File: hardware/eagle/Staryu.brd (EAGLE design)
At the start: 57.1 x 38.1 mm, 29 parts, among them IC1 ATMEGA32U2-TQFP, SW1 CHERRY-MX-LED, SW2 CHERRY-MX-LED, SW3 CHERRY-MX-LED, SW4 CHERRY-MX-LED, SW5 CHERRY-MX-LED, Y1 16MHZ

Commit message: Update eagle files and schematics to v1.2 - Change 3 LEDs on top side to WS2812B
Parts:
- removed D2, D3: (no value), SparkFun-LED:LED-1206
- removed R10, R11, R9: 330, SparkFun-Resistors:0603-RES
- added C5: 0.1uF, SparkFun-Capacitors:0603-CAP
- D1: value (none) -> WS2812B; device SparkFun-LED:LED-1206 -> SparkFun-LED:WS2812B
- JP2: value (none) -> AVR_ISP
- moved LOGO1 30.7 mm to (47.6, 19.1), flipped to the bottom
- moved D1 4.49 mm to (9.53, 25.4), turned to 180 degrees
- moved C2 0.64 mm to (17.8, 35.6)
- moved JP1 0.63 mm to (9.53, 36.8)
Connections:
- removed net N$20: IC1.19, R10.1
- removed net N$21: IC1.20, R9.1
- removed net N$27: D3.C, R11.2
- removed net N$28: D2.C, R10.2
- removed net N$29: D1.C, R9.2
- net 5V: now also C5.1, D1.1; no longer D1.A, D2.A, D3.A
- net GND: now also C5.2, D1.3
- net N$19: now also D1.4, IC1.21; no longer IC1.18, R11.1
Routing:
- net GND: track 185.2 -> 191.6 mm, vias 4 -> 5
- net N$20: track 5.64 -> 0.00 mm, vias 1 -> 0
- net N$19: track 9.91 -> 5.17 mm
- net N$21: track 4.18 -> 0.00 mm, vias 1 -> 0
- net 5V: track 192.6 -> 189.1 mm, vias 3 -> 4
- net N$29: track 2.09 -> 0.00 mm
- net N$28: track 2.09 -> 0.00 mm
- net N$27: track 2.09 -> 0.00 mm
- net N$3: track 4.64 -> 5.20 mm
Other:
- board text added: "Staryu v1.1"

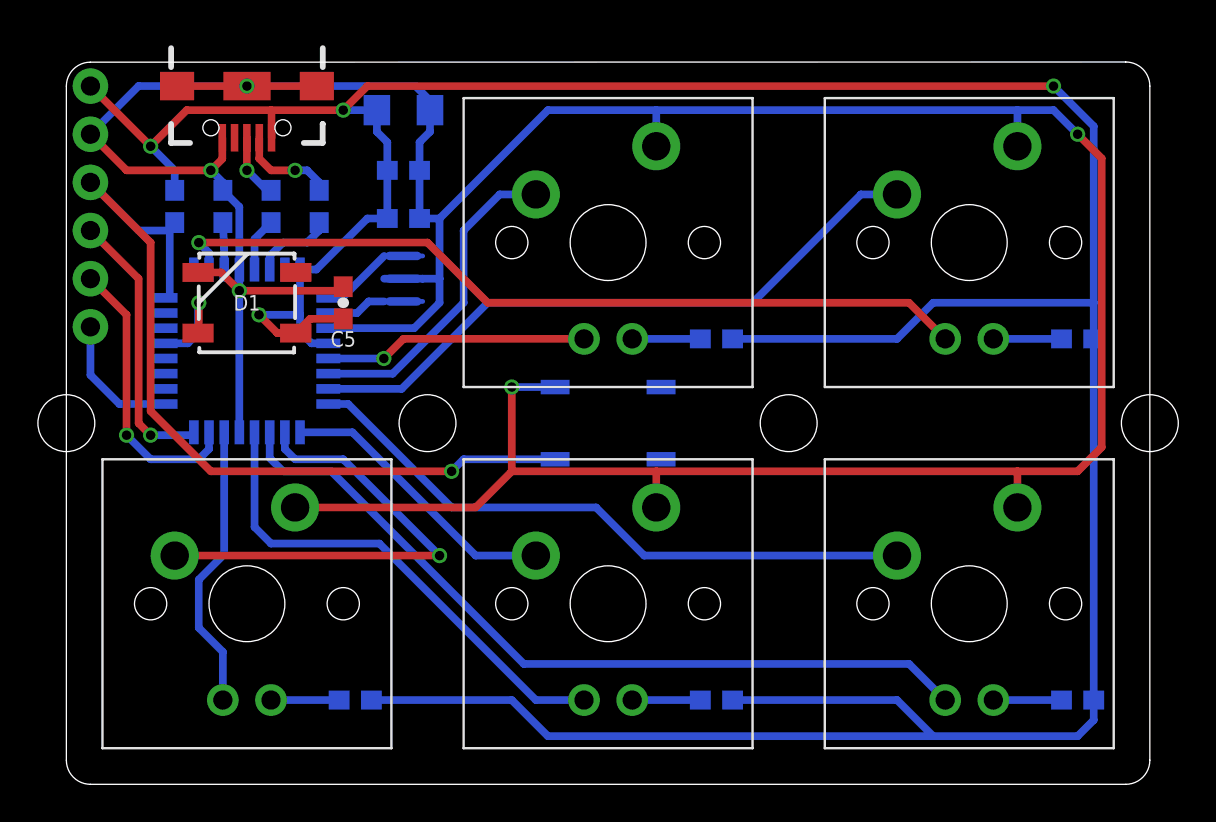
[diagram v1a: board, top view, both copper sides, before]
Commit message: Update eagle files and schematics to v1.2 - Compact outline - Relocate LED and re-route circuits - Add logos
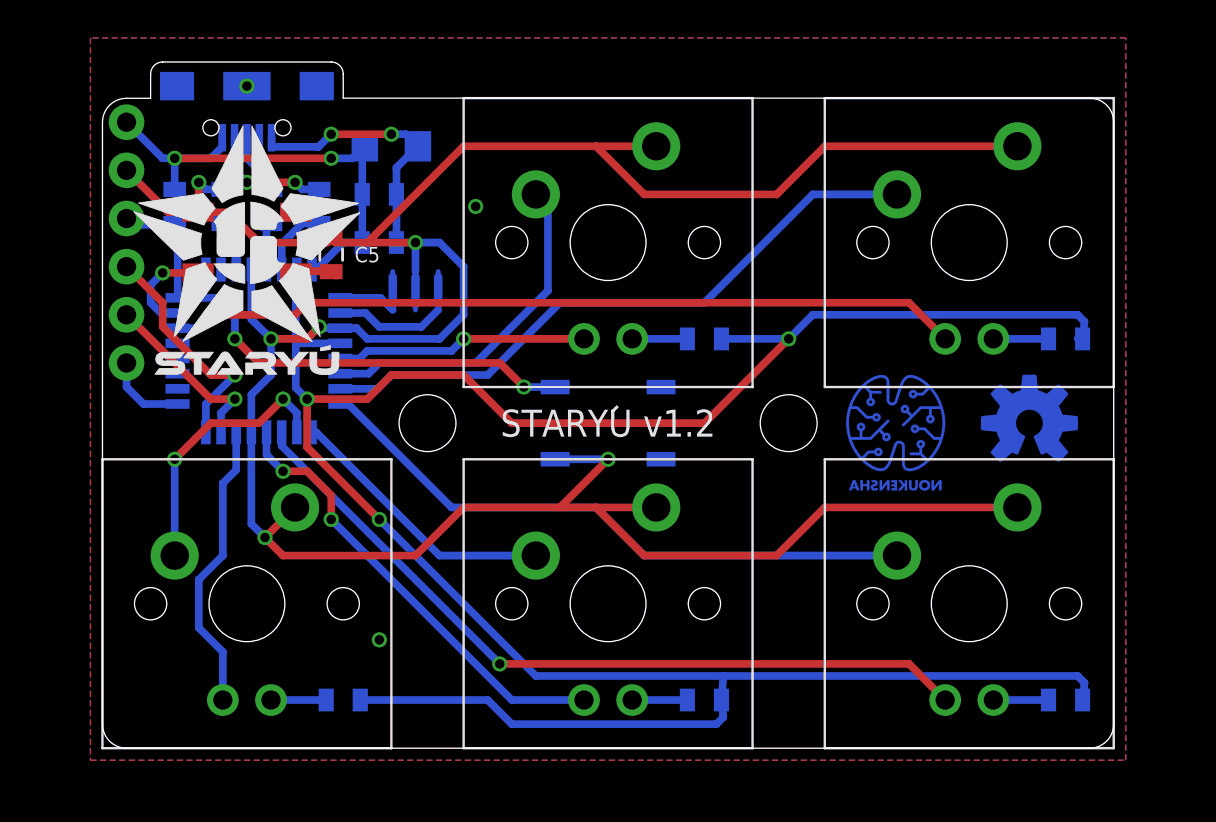
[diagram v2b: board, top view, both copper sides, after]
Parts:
- removed IC1: ATMEGA32U2-TQFP, adafruit:TQFP32-08
- added LOGO2: NOUKENSHA-LOGOM, Noukensha:NOUKENSHA-LOGO-M
- added LOGO3: OSHW-LOGOM, Noukensha:OSHW-LOGO-M
- added U$3: CC-BY-SANIX, cc-by-sa:CC-BY-SA_NIX
- added U1: ATMEGA32U2-TQFP, adafruit:TQFP32-08
- C1, C3, C4, C5: device SparkFun-Capacitors:0603-CAP -> SparkFun-Capacitors:0805
- D1: device SparkFun-LED:WS2812B -> ws2812:WS2812B_NOSILK
- LOGO1: value OSHW-LOGOM -> STARYU-LOGO; device SparkFun-Aesthetics:OSHW-LOGO-M -> Noukensha:STARYU-LOGO
- R1, R2, R3, R4, R5, R6, R7, R8: device SparkFun-Resistors:0603-RES -> SparkFun-Resistors:0805
- moved LOGO1 39.3 mm to (9.53, 28.6), flipped to the top
- moved D1 3.18 mm to (9.53, 28.6)
- moved JP2 2.69 mm to (3.17, 34.9)
- moved C5 2.62 mm to (14.0, 27.9)
- moved C2 2.01 mm to (17.1, 33.7)
- moved C3 1.80 mm to (16.5, 31.1)
- moved C4 1.80 mm to (16.5, 28.6)
- moved Y1 0.90 mm to (18.4, 26.0), turned to 180 degrees
- moved R5 0.64 mm to (52.7, 23.5)
- moved R6 0.64 mm to (52.7, 4.45)
- moved R8 0.63 mm to (14.6, 4.45)
- moved R4 0.63 mm to (33.7, 23.5)
- moved R7 0.63 mm to (33.7, 4.45)
- flipped JP1 to the bottom
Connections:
- new net SHIELD: JP1.SHIELD1, JP1.SHIELD2, JP1.SHIELD3
- net 5V: now also U1.31, U1.32, U1.4; no longer IC1.31, IC1.32, IC1.4
- net GND: now also S1.1, U1.13, U1.28, U1.3; no longer IC1.13, IC1.28, IC1.3, JP1.SHIELD1, JP1.SHIELD2, JP1.SHIELD3, S1.3
- net MISO: now also U1.17; no longer IC1.17
- net MOSI: now also U1.16; no longer IC1.16
- net N$1: now also U1.29; no longer IC1.29
- net N$14: now also U1.6; no longer IC1.6
- net N$15: now also U1.7; no longer IC1.7
- net N$16: now also U1.8; no longer IC1.8
- net N$17: now also U1.9; no longer IC1.9
- net N$18: now also U1.10; no longer IC1.10
- net N$19: now also U1.23; no longer IC1.21
- net N$2: now also U1.30; no longer IC1.30
- net N$30: now also U1.12; no longer IC1.12
- net N$31: now also U1.22; no longer IC1.26
- net N$32: now also U1.11; no longer IC1.11
- net N$33: now also U1.14; no longer IC1.14
- net N$34: now also U1.5; no longer IC1.5
- net N$5: now also U1.1; no longer IC1.1
- net N$6: now also U1.2; no longer IC1.2
- net N$7: now also U1.27; no longer IC1.27
- net N$8: now also S1.3, U1.24; no longer IC1.24, S1.1
- net SCK: now also U1.15; no longer IC1.15
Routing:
- net 5V: track 189.1 -> 161.7 mm, vias 4 -> 6
- net GND: track 191.6 -> 165.8 mm, vias 5 -> 8
- net N$8: track 45.9 -> 29.2 mm, vias 1 -> 2
- net N$18: track 25.3 -> 14.2 mm, vias 1 -> 2
- net SCK: track 15.0 -> 9.61 mm
- net MISO: track 7.25 -> 4.33 mm
- net N$6: track 3.20 -> 5.83 mm
- net N$30: track 26.2 -> 24.0 mm, vias 0 -> 2
- net MOSI: track 14.5 -> 12.5 mm
- net N$3: track 5.20 -> 6.60 mm, vias 1 -> 2
- net N$31: track 43.1 -> 41.8 mm
- net N$32: track 42.3 -> 41.3 mm, vias 0 -> 1
- net N$14: track 17.1 -> 18.1 mm
- net N$5: track 3.86 -> 3.03 mm
- net N$11: track 3.59 -> 2.91 mm
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- added copper zone on layer 1, net SHIELD
- added copper zone on layer 16, net SHIELD
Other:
- board size 57.1 x 38.1 mm -> 53.3 x 36.2 mm
- board text added: "STARYU v1.2"
- board text removed: "Staryu v1.1"

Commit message: Update eagle files and schematics to v1.3 - Contract outline even more - Change logo to exposing copper - Change footprint of resonator to be easier to solder
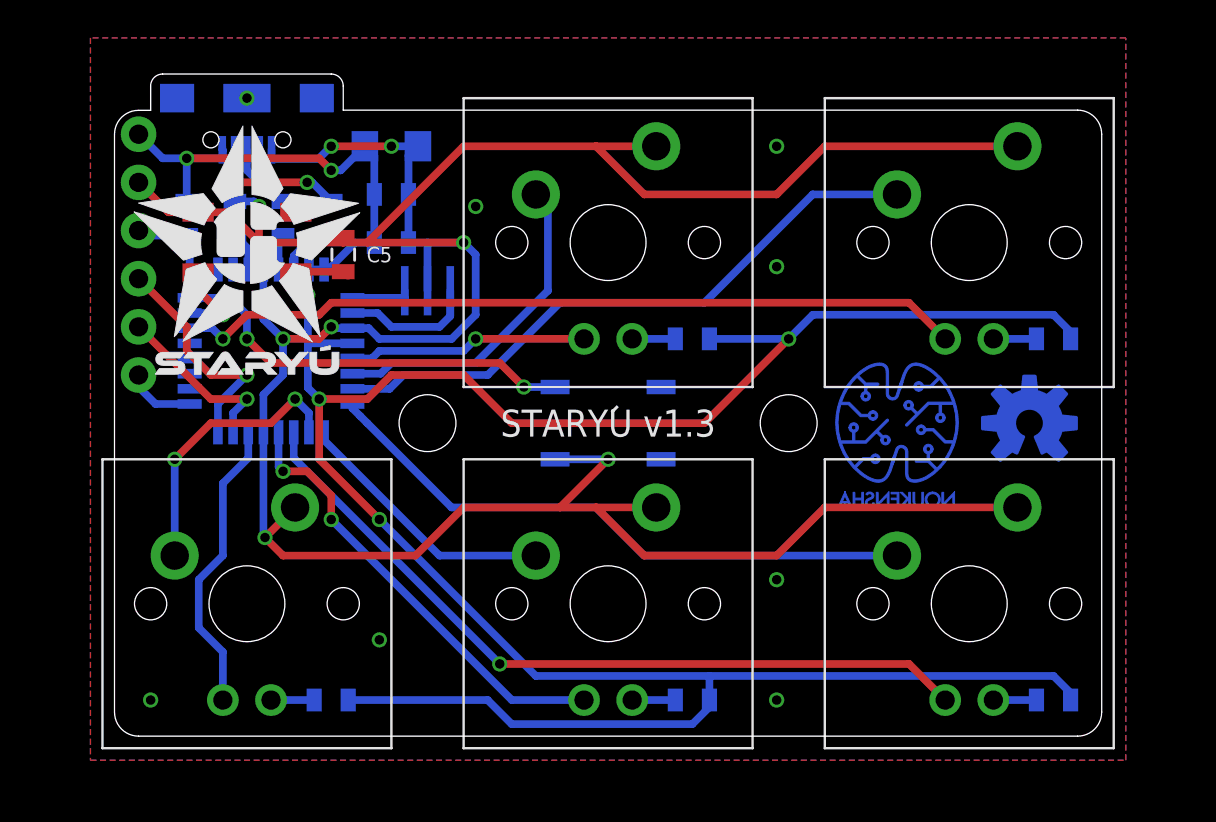
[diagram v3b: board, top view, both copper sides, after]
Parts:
- LOGO1: value STARYU-LOGO -> STARYU_LOGO; device Noukensha:STARYU-LOGO -> Noukensha:STARYU_LOGO
- LOGO2: value NOUKENSHA-LOGOM -> NOUKENSHA_LOGO.3_EXP; device Noukensha:NOUKENSHA-LOGO-M -> Noukensha:NOUKENSHA_LOGO_COPPER_EXPOSED_.3
- LOGO3: value OSHW-LOGOM -> OSHW_LOGOM_EXP; device Noukensha:OSHW-LOGO-M -> Noukensha:OSHW_LOGO_COPPER_EXPOSED_M
- Y1: device SparkFun-FreqCtrl:RESONATOR-SMD -> cstce-resonator:CSTER12M
- moved C1 0.90 mm to (8.89, 29.8)
- moved R1 0.90 mm to (14.0, 29.8)
- moved R2 0.90 mm to (11.4, 29.8)
- moved R3 0.90 mm to (6.35, 29.8)
- moved JP2 0.90 mm to (3.81, 34.3)
- moved Y1 0.64 mm to (19.1, 26.0)
- moved C5 0.63 mm to (14.6, 27.9)
- moved R8 0.63 mm to (14.0, 4.45)
- moved U1 0.63 mm to (10.8, 22.9)
- moved C3 0.63 mm to (17.1, 31.1)
- moved C4 0.63 mm to (17.1, 28.6)
- moved JP1 0.63 mm to (9.53, 36.2)
- moved R4 0.63 mm to (33.0, 23.5)
- moved R5 0.63 mm to (52.1, 23.5)
- moved R6 0.63 mm to (52.1, 4.45)
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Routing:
- net GND: track 165.8 -> 168.3 mm
- net 5V: track 161.7 -> 159.6 mm
- net N$8: track 29.2 -> 28.0 mm
- net N$6: track 5.83 -> 7.04 mm
- net N$19: track 5.35 -> 4.54 mm
- net N$9: track 2.91 -> 2.27 mm
- net N$12: track 2.91 -> 2.27 mm
- net MISO: track 4.33 -> 3.70 mm
- net N$34: track 13.3 -> 12.6 mm
- net N$14: track 18.1 -> 17.5 mm
- net N$13: track 2.91 -> 2.28 mm
- net N$7: track 2.72 -> 2.08 mm
- net N$1: track 2.50 -> 1.87 mm
- net N$2: track 3.77 -> 3.14 mm
- net N$18: track 14.2 -> 14.8 mm
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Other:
- board size 53.3 x 36.2 mm -> 52.1 x 34.9 mm
- board text added: "STARYU v1.3"
- board text removed: "STARYU v1.2"

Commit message: Update hardware to v1.4 - Support both of ATMEGA32U2-AU (32-TQFP) and ATMEGA32U2-MU (32-QFN) - Support both of normal and reverse mounting switch (selected by jumper) - Replace Micro USB connector with a much tougher one - Add a new DOUT connector exported from WS2812B - Correct name and value of Y1 - Change logo
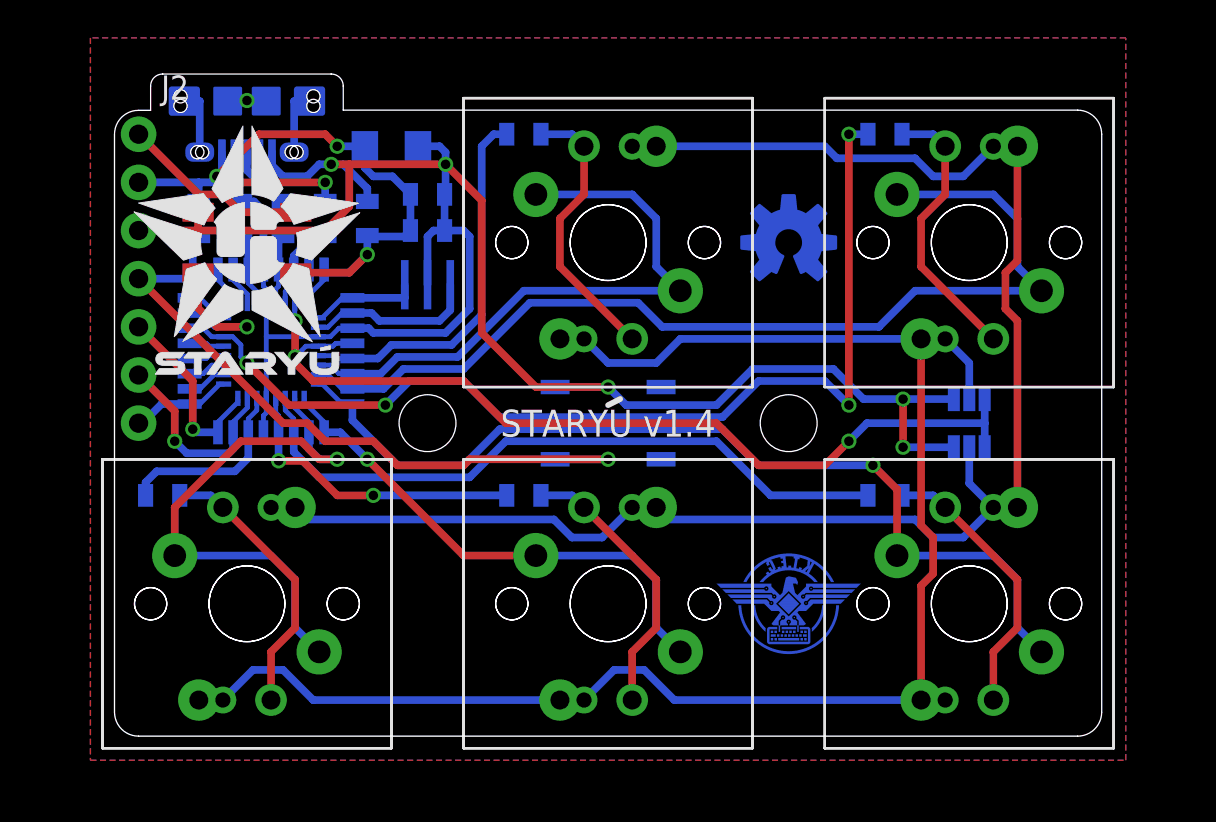
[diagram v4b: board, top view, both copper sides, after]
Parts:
- removed LOGO2: NOUKENSHA_LOGO.3_EXP, Noukensha:NOUKENSHA_LOGO_COPPER_EXPOSED_.3
- added IC1: ATMEGA32U2-QFN, atmega32u2:QFN32
- added J1: MYCON2_USB-MINI-B, usb-micro-b:CON2_USB_MICRO_B_AT
- added J2: (no value), SparkFun-Connectors:1X01_NO_SILK
- added J3: AVR_ISP, SparkFun-Connectors:1X06_NO_SILK
- added SW1-2, SW2-2, SW3-2, SW4-2, SW5-2: CHERRY-MX-LED-MOD, cherrymx:CHERRY-MX-LED-MOD
- added U$1: K.T.E.C._LOGO.3_INCH_EXP, logo:K.T.E.C._LOGO_COPPER_EXPOSED_.3
- C1, C3: device SparkFun-Capacitors:0805 -> SparkFun-Capacitors:0805-CAP
- JP1: value USB_MICROB_PLUGCONN-11752 -> JUMPER-PAD-3-2OF3_NC_BY_PASTE; device SparkFun-Connectors:USB-B-MICRO-SMD_V03 -> SparkFun-Passives:PAD-JUMPER-3-2OF3_NC_BY_PASTE_YES_SILK_FULL_BOX
- JP2: value AVR_ISP -> JUMPER-PAD-3-2OF3_NC_BY_PASTE; device SparkFun-Connectors:1X06_NO_SILK -> SparkFun-Passives:PAD-JUMPER-3-2OF3_NC_BY_PASTE_YES_SILK_FULL_BOX
- SW1, SW2, SW3, SW4, SW5: value CHERRY-MX-LED -> CHERRY-MX-LED-MOD; device cherrymx:CHERRY-MX-LED -> cherrymx:CHERRY-MX-LED-MOD
- U1: device adafruit:TQFP32-08 -> atmega32u2:TQFP32-08
- Y1: device cstce-resonator:CSTER12M -> cst-resonator:CST
- moved JP2 46.8 mm to (47.6, 17.8), flipped to the bottom, turned to 180 degrees
- moved JP1 41.3 mm to (47.6, 20.3), turned to 0 degrees
- moved U$3 25.6 mm to (38.1, 27.0)
- moved LOGO3 15.9 mm to (38.1, 28.6)
- moved R7 14.0 mm to (24.1, 15.2), turned to 0 degrees
- moved R4 14.0 mm to (24.1, 34.3), turned to 0 degrees
- moved R6 14.0 mm to (43.2, 15.2), turned to 0 degrees
- moved R8 14.0 mm to (5.08, 15.2), turned to 0 degrees
- moved R5 14.0 mm to (43.2, 34.3), turned to 0 degrees
- moved C5 2.29 mm to (15.9, 29.8), flipped to the bottom
- moved C4 2.01 mm to (19.1, 29.2)
- moved C3 1.91 mm to (19.1, 31.1)
- moved R3 0.64 mm to (6.99, 29.8)
- moved R1 0.32 mm to (13.7, 29.8)
- moved C1 0.32 mm to (9.21, 29.8)
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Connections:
- removed net N$14: SW1.SW1, U1.6
- removed net N$15: SW2.SW1, U1.7
- removed net N$16: SW3.SW1, U1.8
- removed net N$17: SW4.SW1, U1.9
- removed net N$18: SW5.SW1, U1.10
- removed net N$19: D1.4, U1.23
- removed net N$30: SW4.LED1, U1.12
- removed net N$31: SW2.LED1, U1.22
- removed net N$32: SW3.LED1, U1.11
- removed net N$33: SW5.LED1, U1.14
- removed net N$34: SW1.LED1, U1.5
- new net JP1: JP1.2, SW1-2.SW2, SW1.LED1, SW2-2.SW2, SW2.LED1, SW3-2.SW2, SW3.LED1, SW4-2.SW2, SW4.LED1, SW5-2.SW2, SW5.LED1
- new net JP2: JP2.2, SW1-2.LED1, SW1.SW2, SW2-2.LED1, SW2.SW2, SW3-2.LED1, SW3.SW2, SW4-2.LED1, SW4.SW2, SW5-2.LED1, SW5.SW2
- new net LED1: IC1.5, R4.2, U1.5
- new net LED2: IC1.22, R5.2, U1.22
- new net LED3: IC1.11, R6.2, U1.11
- new net LED4: IC1.12, R7.2, U1.12
- new net LED5: IC1.14, R8.2, U1.14
- new net N$20: IC1.18, U1.18
- new net N$21: IC1.19, U1.19
- new net N$22: IC1.20, U1.20
- new net N$23: IC1.21, U1.21
- new net N$24: IC1.26, U1.26
- new net N$25: IC1.25, U1.25
- new net N$29: R4.1, SW1-2.LED2, SW1.LED2
- new net RGB: D1.4, IC1.23, U1.23
- new net SW1: IC1.6, SW1-2.SW1, SW1.SW1, U1.6
- new net SW2: IC1.7, SW2-2.SW1, SW2.SW1, U1.7
- new net SW3: IC1.8, SW3-2.SW1, SW3.SW1, U1.8
- new net SW4: IC1.9, SW4-2.SW1, SW4.SW1, U1.9
- new net SW5: IC1.10, SW5-2.SW1, SW5.SW1, U1.10
- net 5V: now also IC1.31, IC1.32, IC1.4, J1.P1, J3.1, JP1.1, JP2.3; no longer JP1.VBUS1, JP2.1, R4.2, R5.2, R6.2, R7.2, R8.2
- net GND: now also IC1.13, IC1.28, IC1.3, J1.P5, J3.2, JP1.3, JP2.1, S1.3; no longer JP1.GND1, JP2.2, S1.1, SW1.SW2, SW2.SW2, SW3.SW2, SW4.SW2, SW5.SW2
- net MISO: now also IC1.17, J3.6; no longer JP2.6
- net MOSI: now also IC1.16, J3.4; no longer JP2.4
- net N$1: now also IC1.29
- net N$10: now also SW2-2.LED2
- net N$11: now also SW3-2.LED2
- net N$12: now also SW4-2.LED2
- net N$13: now also SW5-2.LED2
- net N$2: now also IC1.30
- net N$3: now also J1.P2; no longer JP1.D-1
- net N$4: now also J1.P3; no longer JP1.D+1
- net N$5: now also IC1.1
- net N$6: now also IC1.2
- net N$7: now also IC1.27
- net N$8: now also IC1.24, J3.3, S1.1; no longer JP2.3, S1.3
- net N$9: now also D1.2, J2.1; no longer R4.1, SW1.LED2
- net SCK: now also IC1.15, J3.5; no longer JP2.5
- net SHIELD: now also J1.S1, J1.S2, J1.S3, J1.S4, J1.S5, J1.S6; no longer JP1.SHIELD1, JP1.SHIELD2, JP1.SHIELD3
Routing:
- net JP2: track 0.00 -> 86.9 mm
- net JP1: track 0.00 -> 86.6 mm
- net 5V: track 159.6 -> 85.7 mm
- net GND: track 168.3 -> 113.4 mm, vias 8 -> 5
- net LED2: track 0.00 -> 54.7 mm, vias 0 -> 4
- net SW2: track 0.00 -> 52.9 mm
- net SW3: track 0.00 -> 49.6 mm, vias 0 -> 1
- net N$31: track 41.7 -> 0.00 mm, vias 1 -> 0
- net N$32: track 41.0 -> 0.00 mm, vias 1 -> 0
- net LED3: track 0.00 -> 35.8 mm
- net N$15: track 33.0 -> 0.00 mm
- net SW1: track 0.00 -> 32.3 mm
- net N$16: track 32.2 -> 0.00 mm
- net SW5: track 0.00 -> 28.9 mm, vias 0 -> 1
- net SW4: track 0.00 -> 27.3 mm, vias 0 -> 1
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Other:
- board text added: "DO"
- board text added: "N"
- board text added: "R"
- board text added: "STARYU v1.4"
- board text removed: "STARYU v1.3"
